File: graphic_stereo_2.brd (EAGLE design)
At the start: 109 x 29.5 mm, 73 parts, among them IC1 NE5532D, IC2 NE5532D, IC3 NE5532D, IC4 NE5532D, IC5 NE5532D

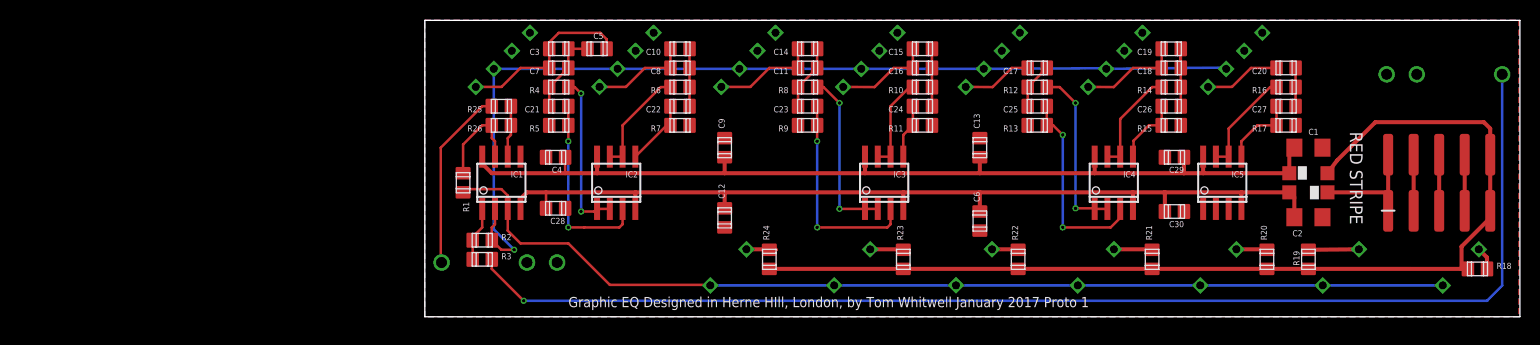
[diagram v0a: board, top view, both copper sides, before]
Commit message: Creating experimental stereo output versions
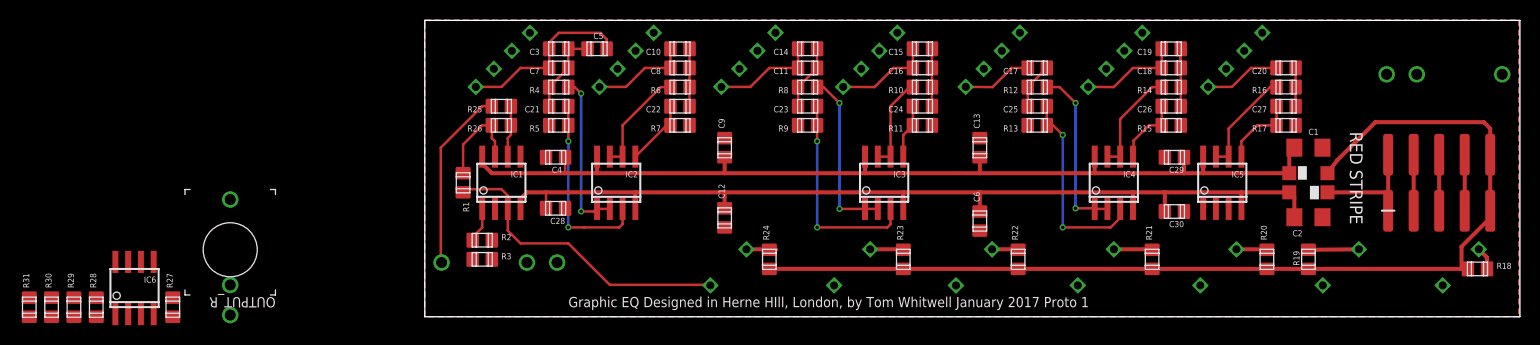
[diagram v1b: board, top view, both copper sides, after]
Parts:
- added IC6: NE5532D, linear:SO08
- added OUTPUT_R: THONKICONNNEW, MusicThingModular:WQP-PJ301M-12_JACK
- added R27, R28: 2.7k, we-rcl:C0805
- added R29, R30: 10k, we-rcl:C0805
- added R31: 470R, we-rcl:C0805
- renumbered OUTPUT to OUTPUTL/MONO
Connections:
- new net N$1: 160HZ.3, 1KHZ.3, 7.7KHZ.3, IC6.3, R27.1
- new net N$22: 160HZ.1, 1KHZ.1, 7.7KHZ.1, IC6.2, R28.1
- new net N$44: IC6.1, R28.2, R3.2
- new net N$46: 16KHZ.1, 2.5KHZ.1, 410HZ.1, 63HZ.1, IC1.2, R2.1
- new net N$47: IC5.3, R29.1, R30.1
- new net N$48: IC5.1, IC5.2, R31.2
- new net N$49: OUTPUTL/MONO.P$1_TIP, R31.1
- new net V+: IC6.8
- new net V-: IC6.4
- net N$3: no longer 160HZ.3, 1KHZ.3, 7.7KHZ.3
- net N$45: now also R27.2
- net N$5: now also R30.2; no longer R3.2
- net N$6: now also OUTPUT_R.P$1_TIP; no longer OUTPUTL/MONO.P$1_TIP
- net N$7: now also OUTPUT_R.P$2_SWITCH, R29.2; no longer 160HZ.1, 16KHZ.1, 1KHZ.1, 2.5KHZ.1, 410HZ.1, 63HZ.1, 7.7KHZ.1, IC1.2, R2.1
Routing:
- net N$6: track 124.5 -> 0.00 mm, vias 1 -> 0
- net N$7: track 97.7 -> 0.00 mm, vias 1 -> 0
- net N$3: track 105.0 -> 30.8 mm
- net N$5: track 5.41 -> 3.51 mm
